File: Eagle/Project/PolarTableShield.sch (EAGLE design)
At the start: 57 parts, among them IC2 LM358D, J10 LED + Radio, J11 Programmer, J3 Pi Connection, J5 IR Sensors, J6 Switch A + B, J7 Switch C + D, J8 Switch E + F, J9 ISP, Q1 BC337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

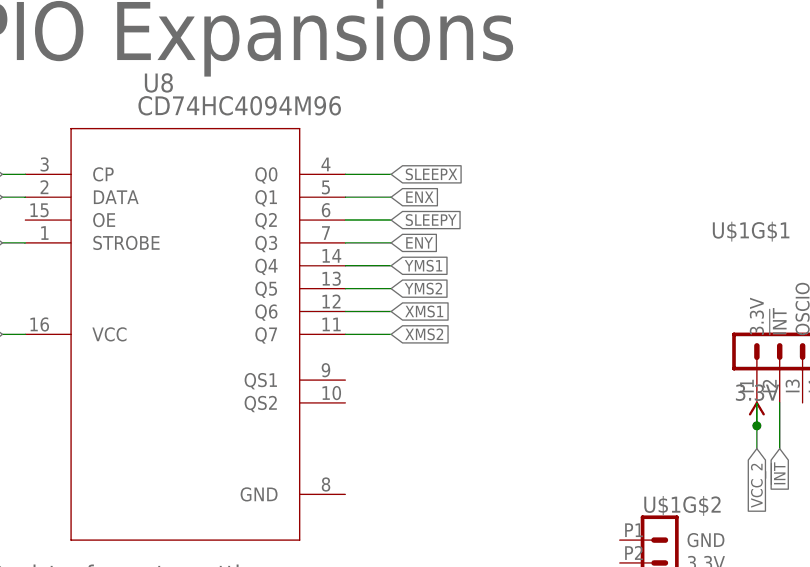
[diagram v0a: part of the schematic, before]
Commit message: Updated motor setting pins to match code.
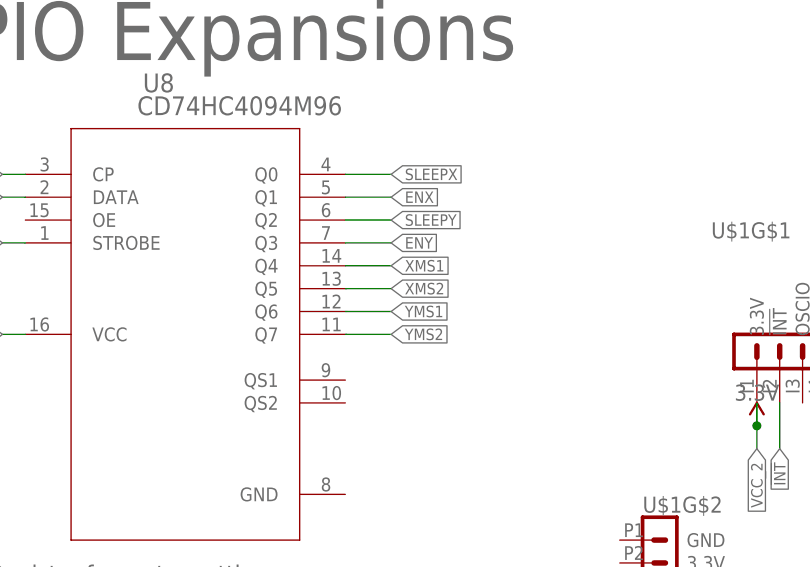
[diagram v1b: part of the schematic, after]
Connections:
- net XMS1: now also U8.Q4; no longer U8.Q6
- net XMS2: now also U8.Q5; no longer U8.Q7
- net YMS1: now also U8.Q6; no longer U8.Q4
- net YMS2: now also U8.Q7; no longer U8.Q5
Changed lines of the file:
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@@
 <segment>
 <pinref part="U8" gate="A" pin="Q3"/>
+<label x="60.96" y="86.36" size="1.27" layer="95" xref="yes"/>
 <wire x1="55.88" y1="86.36" x2="60.96" y2="86.36" width="0.1524" layer="91"/>
-<label x="60.96" y="86.36" size="1.27" layer="95" xref="yes"/>
 </segment>
 </net>
@@
 <segment>
 <pinref part="U8" gate="A" pin="Q2"/>
-<wire x1="55.88" y1="88.9" x2="60.96" y2="88.9" width="0.1524" layer="91"/>
 <label x="60.96" y="88.9" size="1.27" layer="95" xref="yes"/>
+<wire x1="60.96" y1="88.9" x2="55.88" y2="88.9" width="0.1524" layer="91"/>
 </segment>
 </net>
@@
 </segment>
 <segment>
-<pinref part="U8" gate="A" pin="Q4"/>
-<wire x1="55.88" y1="83.82" x2="60.96" y2="83.82" width="0.1524" layer="91"/>
-<label x="60.96" y="83.82" size="1.27" layer="95" xref="yes"/>
+<label x="60.96" y="78.74" size="1.27" layer="95" xref="yes"/>
+<wire x1="56.0324" y1="78.74" x2="60.96" y2="78.74" width="0.1524" layer="91"/>
+<pinref part="U8" gate="A" pin="Q6"/>
+<wire x1="56.0324" y1="78.74" x2="55.88" y2="78.74" width="0.1524" layer="91"/>
 </segment>
 </net>
@@
 </segment>
 <segment>
-<pinref part="U8" gate="A" pin="Q5"/>
-<wire x1="55.88" y1="81.28" x2="60.96" y2="81.28" width="0.1524" layer="91"/>
-<label x="60.96" y="81.28" size="1.27" layer="95" xref="yes"/>
+<label x="60.96" y="76.2" size="1.27" layer="95" xref="yes"/>
+<wire x1="56.0324" y1="76.2" x2="60.96" y2="76.2" width="0.1524" layer="91"/>
+<pinref part="U8" gate="A" pin="Q7"/>
+<wire x1="56.0324" y1="76.2" x2="55.88" y2="76.2" width="0.1524" layer="91"/>
 </segment>
 </net>
@@
 </segment>
 <segment>
-<pinref part="U8" gate="A" pin="Q6"/>
-<wire x1="55.88" y1="78.74" x2="60.96" y2="78.74" width="0.1524" layer="91"/>
-<label x="60.96" y="78.74" size="1.27" layer="95" xref="yes"/>
+<label x="60.96" y="83.82" size="1.27" layer="95" xref="yes"/>
+<pinref part="U8" gate="A" pin="Q4"/>
+<wire x1="60.96" y1="83.82" x2="55.88" y2="83.82" width="0.1524" layer="91"/>
 </segment>
 </net>
@@
 </segment>
 <segment>
-<pinref part="U8" gate="A" pin="Q7"/>
-<wire x1="55.88" y1="76.2" x2="60.96" y2="76.2" width="0.1524" layer="91"/>
-<label x="60.96" y="76.2" size="1.27" layer="95" xref="yes"/>
+<label x="60.96" y="81.28" size="1.27" layer="95" xref="yes"/>
+<wire x1="56.0324" y1="81.28" x2="60.96" y2="81.28" width="0.1524" layer="91"/>
+<pinref part="U8" gate="A" pin="Q5"/>
+<wire x1="55.88" y1="81.28" x2="56.0324" y2="81.28" width="0.1524" layer="91"/>
 </segment>
 </net>
